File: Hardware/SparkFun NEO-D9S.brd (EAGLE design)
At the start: 43.2 x 40.6 mm, 49 parts, among them J1 ANTENNA-SMA-GROUNDEDEDGE_SMA, J2 Qwiic Right Angle, J4 Qwiic Right Angle, U1 U-BLOX_NEO-D9S, U2 3.3V

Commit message: Routed. Add schematic
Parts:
- removed JP5: JUMPER-SMT_3_2-NC_TRACE_SILK, SparkFun-Jumpers:SMT-JUMPER_3_2-NC_TRACE_SILK
- removed U$33: (no value), SparkFun-Aesthetics:SFE_LOGO_FLAME_.1
- added I2C: JUMPER-SMT_3_NO_SILK, SparkFun-Jumpers:SMT-JUMPER_3_NO_SILK
- added LOGO3: SFE_LOGO_NAME_FLAME.1_INCH, SparkFun-Aesthetics:SFE_LOGO_NAME_FLAME_.1
- added LOGO4: OSHW-LOGOS, SparkFun-Aesthetics:OSHW-LOGO-S
- added U$1, U$2, U$3: (no value), output:#GND#0
- added U$10, U$9: (no value), output:#TXD2#3
- added U$11, U$12: (no value), output:#RXD2#0
- added U$13, U$15: (no value), output:#RXD2#3
- added U$16, U$17: (no value), output:BLK0
- added U$18, U$19: (no value), output:GRN0
- added U$20: (no value), output:#5V#0
- added U$21: (no value), output:#5V#6
- added U$22, U$23: (no value), output:#3V3#0
- added U$24, U$25: (no value), output:#3V3#4
- added U$26, U$27: (no value), output:#SDA##CS##0
- added U$28, U$29: (no value), output:#SDA##CS##1
- added U$30, U$31: (no value), output:#TXD1#SDO#0
- added U$32, U$34: (no value), output:#TXD1#SDO#2
- added U$35, U$36: (no value), output:#RXD1#SDI#0
- added U$37, U$38: (no value), output:#RXD1#SDI#2
- added U$39, U$40: (no value), output:#SCL#SCK#0
- added U$4, U$5, U$6: (no value), output:#GND#1
- added U$41, U$42: (no value), output:#SCL#SCK#1
- added U$43: (no value), output:##SAFEBOOT##0
- added U$44: (no value), output:##SAFEBOOT##1
- added U$45: (no value), output:##RESET##0
- added U$46: (no value), output:##RESET##1
- added U$47: (no value), output:#EXT_INT#0
- added U$48: (no value), output:#EXT_INT#1
- added U$49: (no value), output:PWR0
- added U$50: (no value), output:#PWR#0
- added U$51: (no value), output:#SPI#0
- added U$52: (no value), output:#I�C#0
- added U$53: (no value), output:#SHLD#0
- added U$54, U$55: (no value), output:NEO#D9S0
- added U$7, U$8: (no value), output:#TXD2#0
- J3: device SparkFun-Connectors:USB-C-16P -> SparkFun-Connectors:USB-C-16P-2LAYER-PADS
- LOGO1: value OSHW-LOGOMINI -> OSHW-LOGOS; device SparkFun-Aesthetics:OSHW-LOGO-MINI -> SparkFun-Aesthetics:OSHW-LOGO-S
- moved LOGO1 49.9 mm to (5.08, 24.1)
- moved LOGO2 46.9 mm to (14.0, 20.3), turned to 270 degrees
- moved PWR\ 7.62 mm to (38.1, 33.0), turned to 180 degrees
- moved R7 4.32 mm to (17.3, 30.4), turned to 0 degrees
- moved C1 3.81 mm to (33.9, 22.1), turned to 0 degrees
- moved R8 2.51 mm to (17.3, 28.7), turned to 0 degrees
- moved C2 0.25 mm to (16.9, 9.14)
- moved C4 0.25 mm to (23.2, 9.14), turned to 90 degrees
- moved C5 0.25 mm to (25.1, 9.14), turned to 270 degrees
- moved R13 0.13 mm to (4.57, 18.9)
- moved R12 0.13 mm to (4.57, 6.48)
- moved SHLD 0.13 mm to (1.78, 12.7)
- turned R11 to 0 degrees
- turned R6 to 180 degrees
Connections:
- net 3.3V: now also I2C.2; no longer JP5.2
- net D+: now also D2.6; no longer D2.4
- net D-: now also D2.4; no longer D2.6
- net N$5: now also I2C.1; no longer JP5.1
- net N$8: now also I2C.3; no longer JP5.3
- net SHIELD: no longer J3.SHLD5, J3.SHLD6, J3.SHLD7, J3.SHLD8
- net USB_D+: now also D2.1; no longer D2.3
- net USB_D-: now also D2.3; no longer D2.1
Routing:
- net 3.3V: track 0.00 -> 148.3 mm, vias 0 -> 3
- net SCL/SCK: track 0.00 -> 129.4 mm, vias 0 -> 7
- net SDA/!CS!: track 0.00 -> 123.7 mm, vias 0 -> 8
- net RXD1/SDI: track 0.00 -> 86.1 mm, vias 0 -> 1
- net TXD1/SDO: track 0.00 -> 84.3 mm, vias 0 -> 1
- net TXD2: track 0.00 -> 68.2 mm, vias 0 -> 2
- net RXD2: track 0.00 -> 65.6 mm, vias 0 -> 1
- net !SAFEBOOT!: track 0.00 -> 49.9 mm, vias 0 -> 3
- net EXT_INT: track 0.00 -> 43.0 mm
- net 5V: track 0.00 -> 38.1 mm, vias 0 -> 2
- net D-: track 0.00 -> 27.0 mm, vias 0 -> 2
- net D+: track 0.00 -> 26.4 mm, vias 0 -> 2
- net !RESET!: track 0.00 -> 22.1 mm, vias 0 -> 2
- net SHIELD: track 0.00 -> 17.2 mm
- net GND: track 0.00 -> 16.0 mm, vias 0 -> 143
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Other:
- board text added: "Route Out"

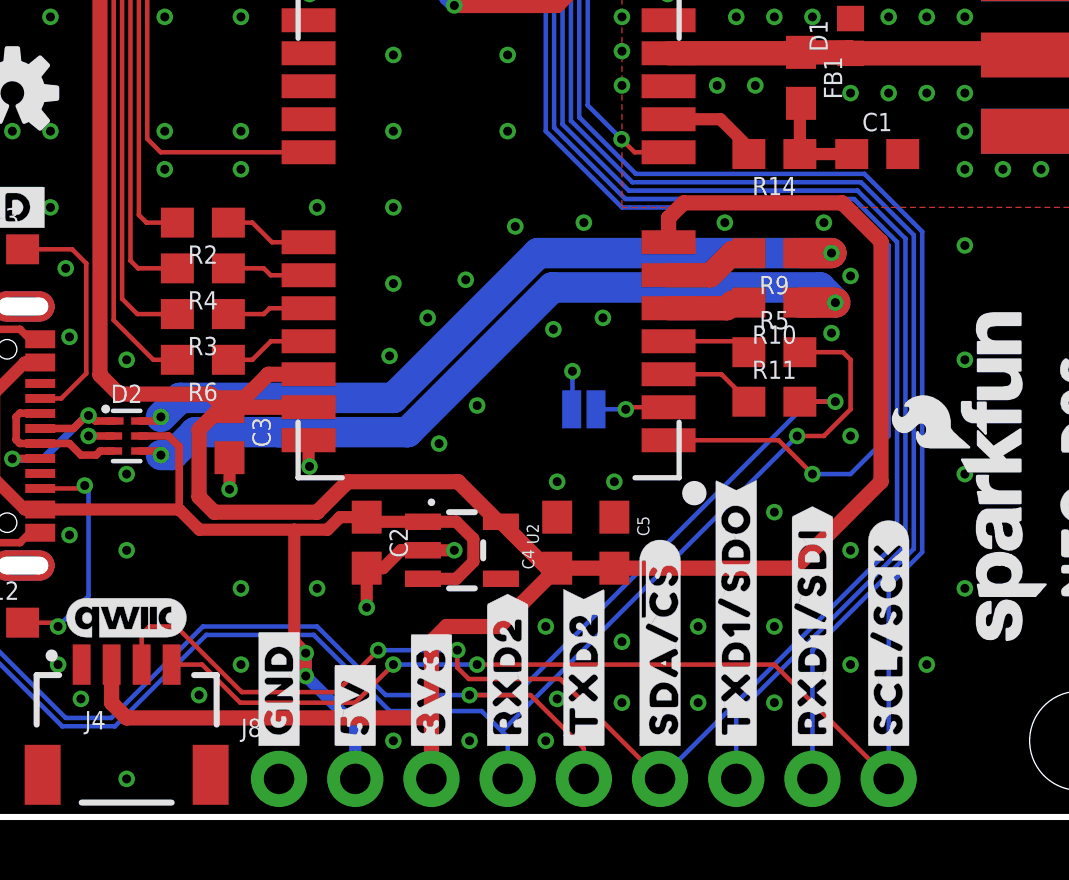
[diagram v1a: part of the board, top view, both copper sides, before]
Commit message: Add C6
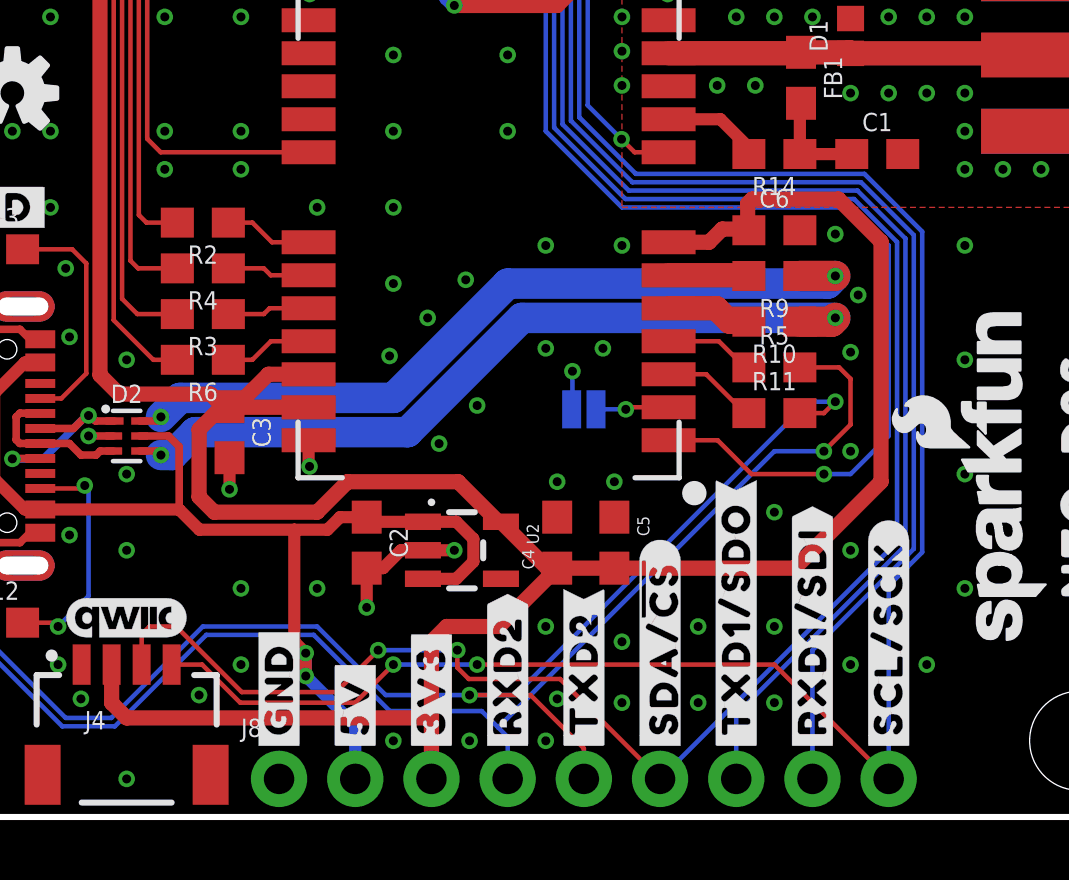
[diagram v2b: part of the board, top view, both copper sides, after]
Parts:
- added C6: 1.0uF, SparkFun-Capacitors:0603
- moved R9 0.76 mm to (30.5, 18.0)
- moved R10 0.63 mm to (30.5, 16.5)
- moved R5 0.51 mm to (30.5, 15.0)
- moved R11 0.38 mm to (30.5, 13.5)
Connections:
- net 3.3V: now also C6.1
- net GND: now also C6.2
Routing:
- net D-: track 27.0 -> 26.4 mm
- net GND: vias 143 -> 142

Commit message: Final tweaks. Ready for proto review.
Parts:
- moved I2C 0.68 mm to (20.3, 28.6)
- moved U$52 0.68 mm to (18.7, 28.6)
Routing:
- net RXD2: track 65.4 -> 66.4 mm
- net !SAFEBOOT!: track 49.9 -> 50.5 mm
- net N$8: track 5.71 -> 5.14 mm
- net N$5: track 5.66 -> 5.13 mm
- net GND: vias 142 -> 143

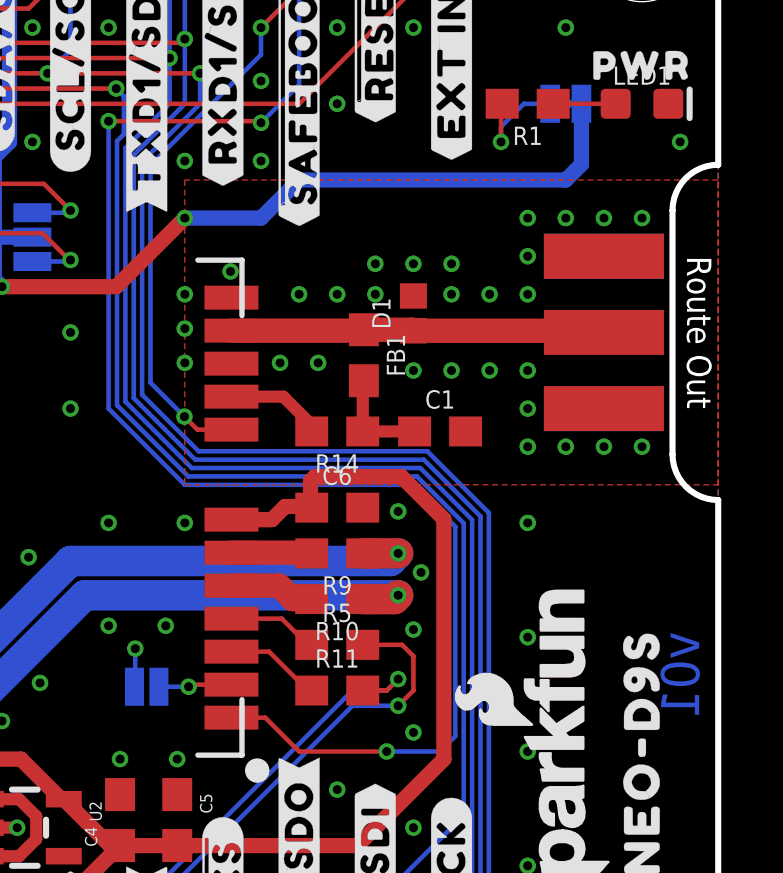
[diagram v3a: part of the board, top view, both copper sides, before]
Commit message: Add cut marks for antenna power
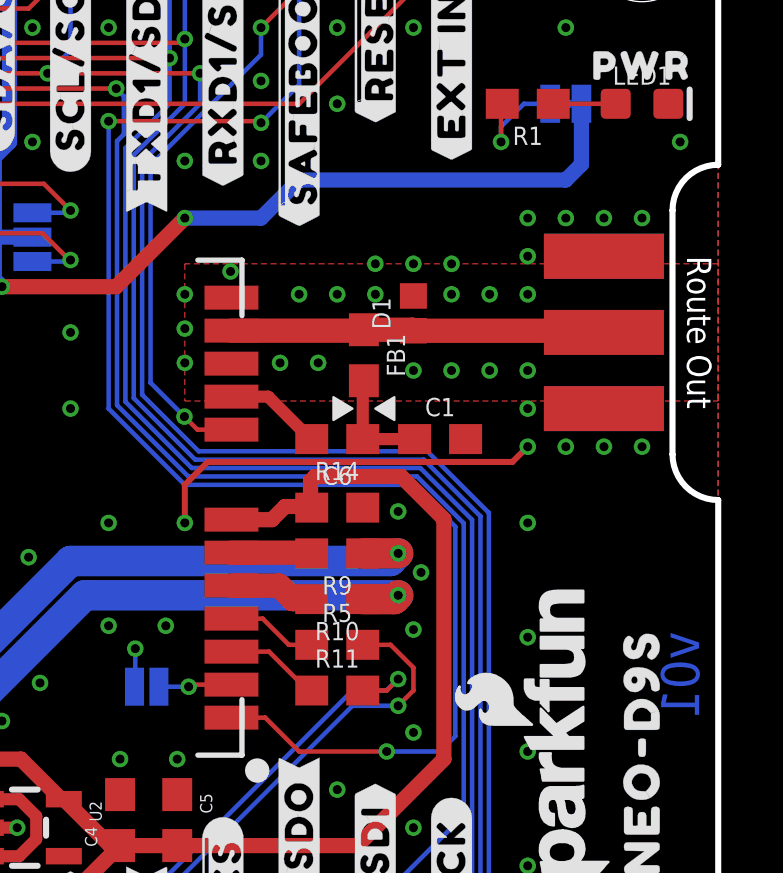
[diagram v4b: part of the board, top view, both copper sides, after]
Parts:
- moved C1 0.25 mm to (33.9, 21.8)
- moved R14 0.25 mm to (30.5, 21.8)
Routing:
- net GND: track 16.0 -> 29.2 mm

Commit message: Post-Proto Review Changes
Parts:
- added U$33: (no value), output:#TXD1#POCI#2
- U$30, U$31: device output:#TXD1#SDO#0 -> output:#TXD1#POCI#0
- U$32: device output:#TXD1#SDO#2 -> output:#TXD1#POCI#2
- U$34: device output:#TXD1#SDO#2 -> output:#RXD1#PICO#0
- U$35: device output:#RXD1#SDI#0 -> output:#RXD1#PICO#0
- U$36: device output:#RXD1#SDI#0 -> output:#RXD1#PICO#2
- U$37: device output:#RXD1#SDI#2 -> output:#RXD1#PICO#2
- U$38: device output:#RXD1#SDI#2 -> SparkFun-Aesthetics:QWIIC_4MM
- moved U$32 39.4 mm to (24.1, 41.1), flipped to the top, turned to 90 degrees
- moved U$35 39.4 mm to (26.7, 41.1), flipped to the bottom, turned to 270 degrees
- moved U$34 37.4 mm to (31.8, 2.03)
- moved LOGO1 28.7 mm to (33.0, 30.5), turned to 90 degrees
- moved U$38 17.9 mm to (8.89, 36.5), turned to 0 degrees
- moved U$52 3.49 mm to (22.1, 29.2)
- moved JP31 2.54 mm to (2.54, 40.6)
- moved JP41 2.54 mm to (40.6, 40.6)
- moved U$23 2.54 mm to (16.5, 41.1)
- moved U$25 2.54 mm to (16.5, 41.1)
- moved U$27 2.54 mm to (19.1, 41.1)
- moved U$29 2.54 mm to (19.1, 41.1)
- moved U$3 2.54 mm to (14.0, 41.1)
- moved U$31 2.54 mm to (24.1, 41.1)
- moved U$36 2.54 mm to (26.7, 41.1), flipped to the top, turned to 90 degrees
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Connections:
- net RXD1/SDI renamed RXD1/PICO
- net TXD1/SDO renamed TXD1/POCI
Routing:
- net RXD2: track 66.1 -> 70.6 mm, vias 1 -> 3
- net SCL/SCK: track 129.5 -> 132.2 mm
- net EXT_INT: track 43.0 -> 45.6 mm
- net !SAFEBOOT!: track 50.5 -> 52.9 mm
- net 3.3V: track 148.8 -> 146.6 mm
- net N$5: track 5.13 -> 2.93 mm
- net !RESET!: track 22.1 -> 24.2 mm
- net RXD1/PICO: track 86.2 -> 88.3 mm
- net SDA/!CS!: track 123.8 -> 125.2 mm
- net N$8: track 5.14 -> 3.72 mm
- net TXD2: track 68.3 -> 69.6 mm, vias 2 -> 3
- net TXD1/POCI: track 84.4 -> 85.2 mm
- net GND: track 29.2 -> 29.0 mm, vias 143 -> 150
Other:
- board size 43.2 x 40.6 mm -> 43.2 x 43.2 mm

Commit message: Add PROD_ID for NEO-D9S-00B. Add Proto production files
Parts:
- U1: value U-BLOX_NEO-D9S -> U-BLOX_NEO-D9S-00B
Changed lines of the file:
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@@
 <attribute name="VALUE" x="30.48" y="18.796" size="0.6096" layer="27" font="vector" ratio="20" align="top-center"/>
 </element>
-<element name="U1" library="SparkFun-GPS" package="NEO-M9N/M8T/M8U/D9S" value="U-BLOX_NEO-D9S" x="20.955" y="19.558" smashed="yes">
+<element name="U1" library="SparkFun-GPS" package="NEO-M9N/M8T/M8U/D9S" value="U-BLOX_NEO-D9S-00B" x="20.955" y="19.558" smashed="yes">
 <attribute name="NAME" x="14.855" y="28.058" size="0.508" layer="25"/>
-<attribute name="PROD_ID" value="IC-" x="20.955" y="19.558" size="1.778" layer="27" font="vector" ratio="15" display="off"/>
+<attribute name="PROD_ID" value="IC-16579" x="20.955" y="19.558" size="1.778" layer="27" font="vector" ratio="15" display="off"/>
 <attribute name="VALUE" x="14.855" y="10.558" size="0.508" layer="27"/>
 </element>

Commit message: Updates for v10 PCB
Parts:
- added 3V3: JUMPER-SMT_2_NC_TRACE_SILK, SparkFun-Jumpers:SMT-JUMPER_2_NC_TRACE_SILK
- added C7: 47pF, SparkFun-Capacitors:0603
- added R15: DNP, SparkFun-Resistors:0603_NO_CREAM
- added U$56, U$57: (no value), output:#3V3#0
- added U$58: (no value), output:#ANT_PWR#0
- added U$59: (no value), output:#ANT_PWR#1
- J7: device SparkFun-Connectors:1X09_NO_SILK -> SparkFun-Connectors:1X10_NO_SILK
- moved R1 16.1 mm to (39.4, 17.1), turned to 0 degrees
- moved PWR\ 15.9 mm to (39.4, 17.1), turned to 0 degrees
- moved U$50 15.9 mm to (41.3, 17.1)
- moved LED1 14.0 mm to (39.4, 19.1)
- moved U$49 14.0 mm to (39.4, 20.3)
- moved LOGO1 8.52 mm to (40.6, 34.3)
- moved D1 1.27 mm to (35.6, 26.0)
- moved LOGO3 1.27 mm to (38.1, 10.2)
- moved U$54 1.27 mm to (40.6, 10.2)
- moved R14 1.02 mm to (31.5, 21.9)
- moved FB1 0.95 mm to (32.3, 24.6)
- moved C1 0.95 mm to (34.9, 21.9)
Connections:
- new net ANT_PWR: J7.10, R15.2
- new net N$13: 3V3.1, J5.3
- new net SMA: C7.1, D1.1, FB1.1, J1.SIG, R15.1
- net 3.3V: now also 3V3.2
- net ANT: now also C7.2; no longer D1.1, FB1.1, J1.SIG
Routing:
- net ANT_PWR: track 0.00 -> 15.7 mm
- net ANT: track 12.5 -> 2.04 mm
- net 3.3V: track 146.6 -> 137.2 mm, vias 3 -> 4
- net SMA: track 0.00 -> 8.75 mm
- net N$13: track 0.00 -> 2.02 mm
- net VCC_RF: track 3.26 -> 4.25 mm
- net N$1: track 3.71 -> 2.94 mm
- net GND: vias 150 -> 159
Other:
- board text added: "v10"
- board text removed: "v01"

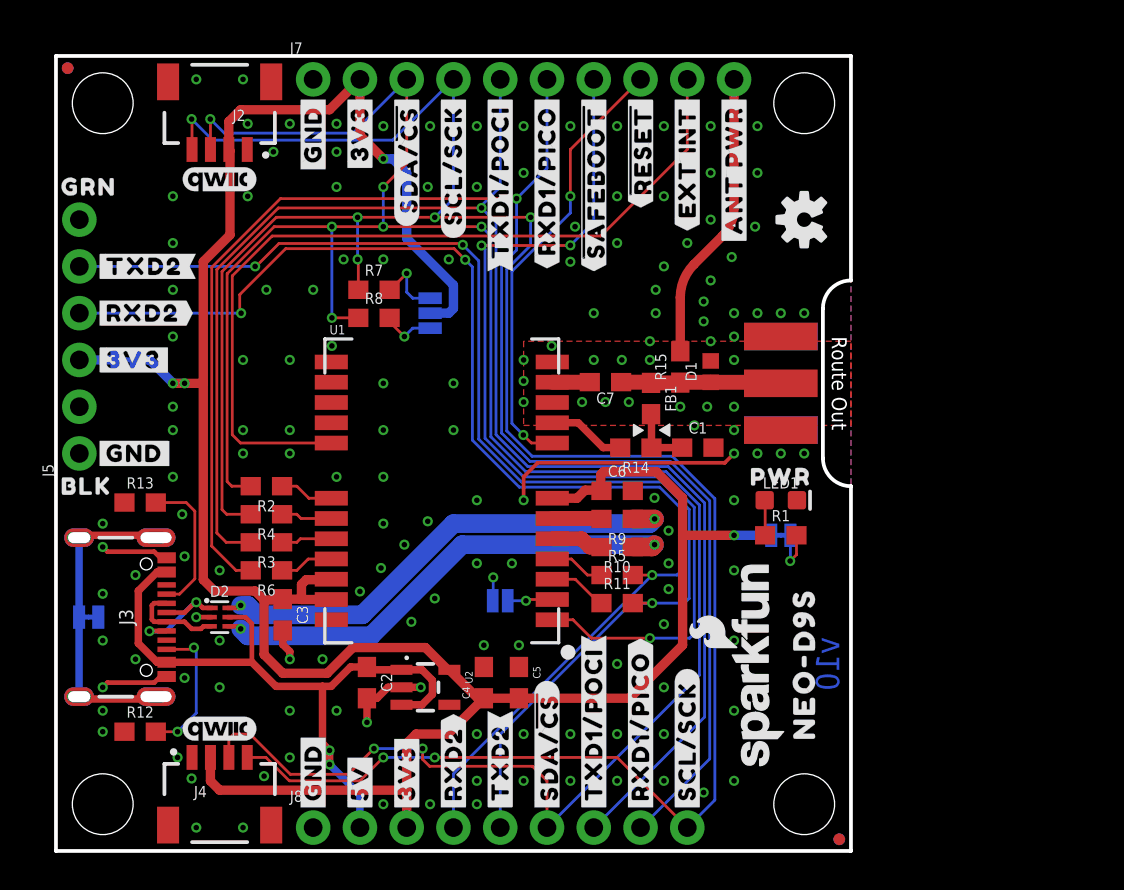
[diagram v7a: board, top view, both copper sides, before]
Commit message: Updates after REDs Review
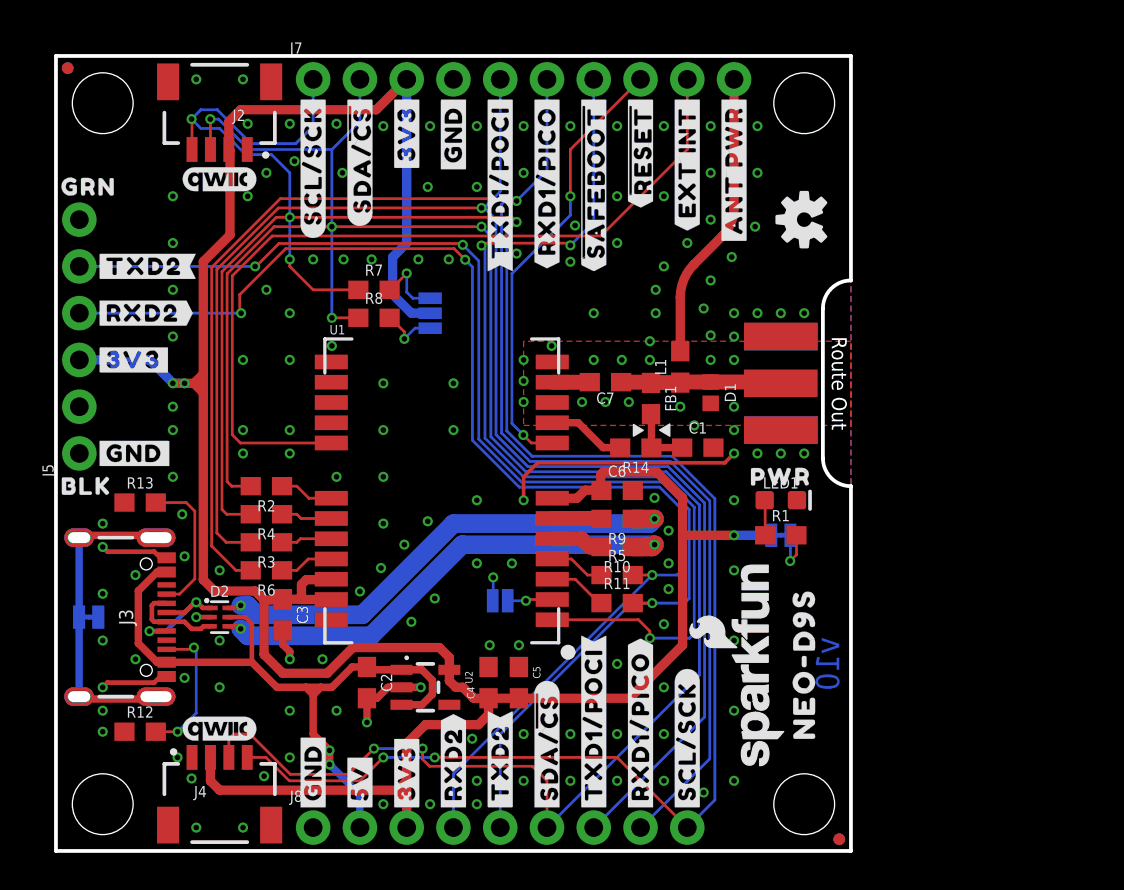
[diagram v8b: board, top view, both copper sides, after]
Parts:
- removed R15: DNP, SparkFun-Resistors:0603_NO_CREAM
- added L1: DNP, SparkFun-Coils:0603_NO-CREAM
- moved U$3 7.62 mm to (21.6, 41.1)
- moved U$4 7.62 mm to (21.6, 41.1)
- moved U$40 7.62 mm to (14.0, 41.1)
- moved U$41 7.62 mm to (14.0, 41.1)
- moved U$23 2.54 mm to (19.1, 41.1)
- moved U$25 2.54 mm to (19.1, 41.1)
- moved U$27 2.54 mm to (16.5, 41.1)
- moved U$29 2.54 mm to (16.5, 41.1)
- moved D1 1.14 mm to (35.6, 24.9), turned to 270 degrees
- moved C4 0.25 mm to (23.5, 9.14)
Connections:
- net 3.3V: now also J7.3; no longer J7.2
- net ANT_PWR: now also L1.2; no longer R15.2
- net GND: now also J7.4; no longer J7.1
- net SCL/SCK: now also J7.1; no longer J7.4
- net SDA/!CS!: now also J7.2; no longer J7.3
- net SMA: now also L1.1; no longer R15.1
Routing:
- net SDA/!CS!: track 125.2 -> 120.4 mm, vias 8 -> 6
- net 3.3V: track 137.2 -> 141.4 mm, vias 4 -> 3
- net SCL/SCK: track 132.2 -> 129.4 mm, vias 7 -> 6
- net 5V: track 38.0 -> 39.0 mm
- net GND: vias 159 -> 161
